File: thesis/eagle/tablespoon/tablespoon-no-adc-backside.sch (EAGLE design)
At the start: 35 parts, among them IC1 7805DT, IC2 7805DT, IC3 TL072D, U2 ADCS7477

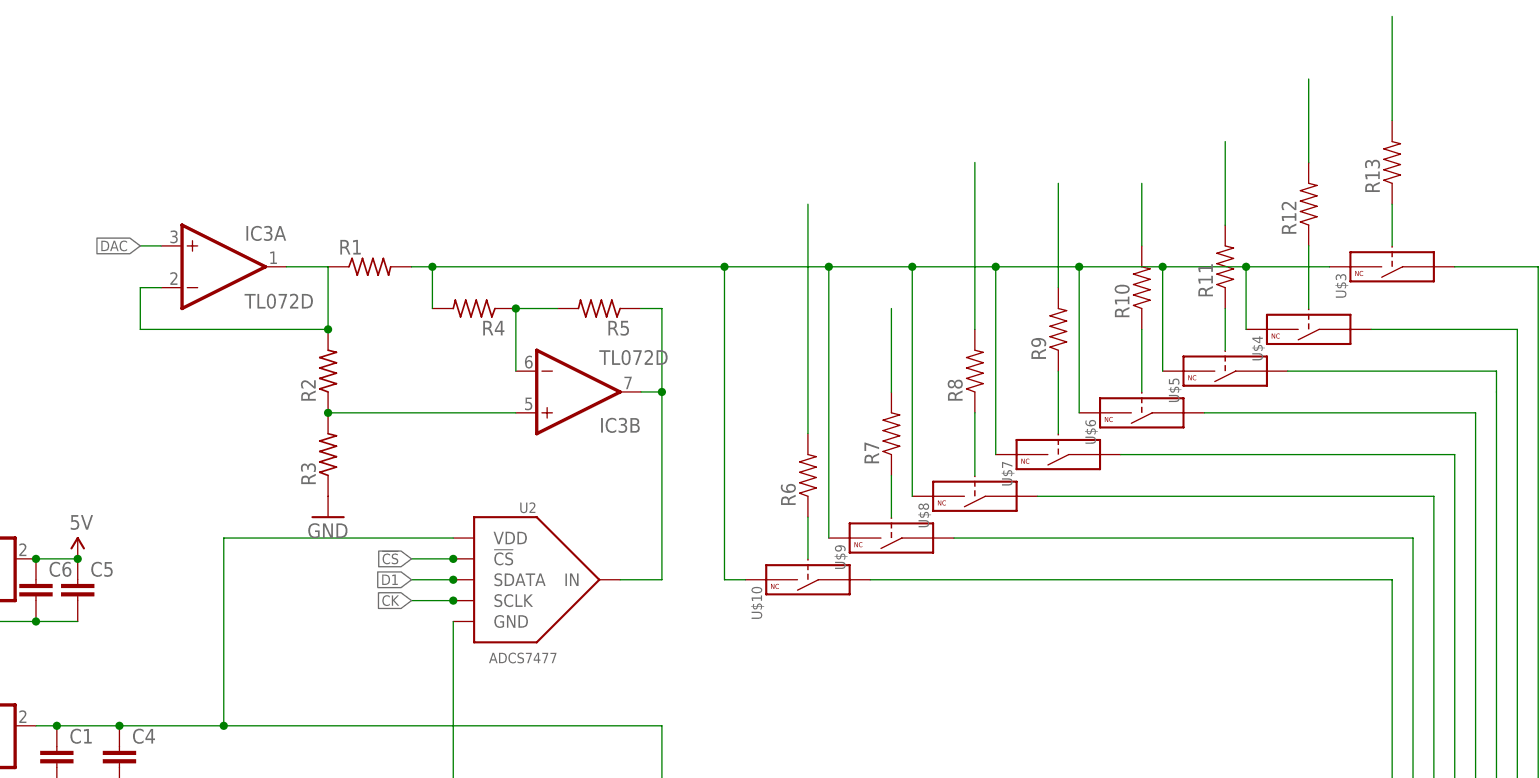
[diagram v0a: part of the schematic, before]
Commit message: fixed lack of resistor divider on current amp
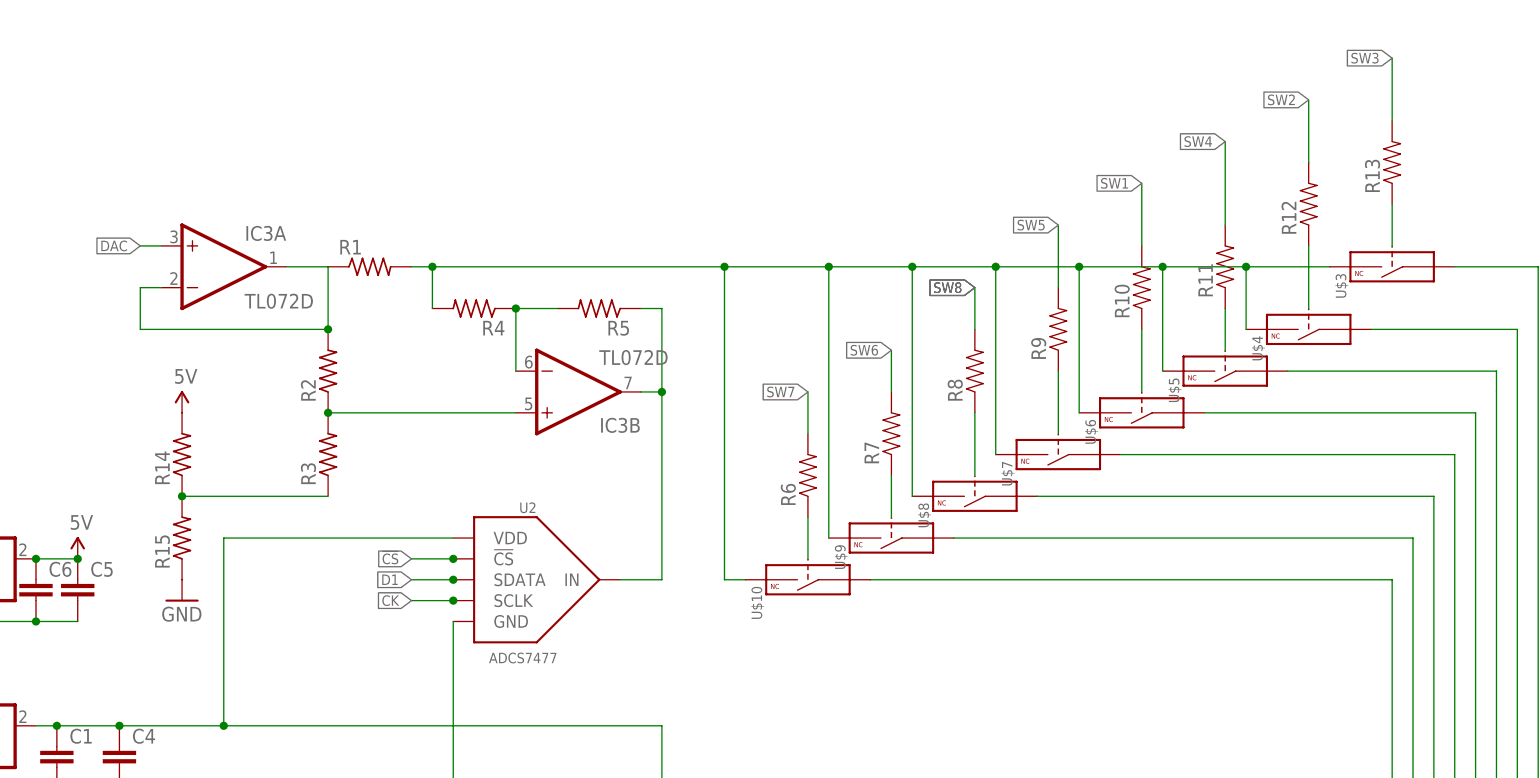
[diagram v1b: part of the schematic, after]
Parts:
- added R14, R15: (no value), rcl:R-US_R0603
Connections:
- new net N$35: R14.1, R15.2, R3.1
- net 5V: now also R14.2
- net GND: now also R15.1; no longer R3.1
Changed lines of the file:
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@@
 <part name="R4" library="rcl" deviceset="R-US_" device="R0603"/>
 <part name="R5" library="rcl" deviceset="R-US_" device="R0603"/>
-<part name="GND7" library="supply1" deviceset="GND" device=""/>
 <part name="U2" library="butter" deviceset="ADCS7477" device=""/>
 <part name="R6" library="SparkFun-Passives" deviceset="RESISTOR" device="0805-RES"/>
@@
 <part name="R10" library="SparkFun-Passives" deviceset="RESISTOR" device="0805-RES"/>
 <part name="GND8" library="supply1" deviceset="GND" device=""/>
+<part name="R14" library="rcl" deviceset="R-US_" device="R0603"/>
+<part name="R15" library="rcl" deviceset="R-US_" device="R0603"/>
+<part name="SUPPLY2" library="SparkFun-Aesthetics" deviceset="5V" device=""/>
+<part name="GND7" library="supply1" deviceset="GND" device=""/>
 </parts>
 <sheets>
@@
 <instance part="R4" gate="G$1" x="81.28" y="134.62" rot="R180"/>
 <instance part="R5" gate="G$1" x="96.52" y="134.62" rot="R180"/>
-<instance part="GND7" gate="1" x="63.5" y="109.22"/>
 <instance part="U2" gate="G$1" x="86.36" y="101.6" rot="MR0"/>
 <instance part="R6" gate="G$1" x="121.92" y="114.3" rot="R90"/>
@@
 <instance part="R10" gate="G$1" x="162.56" y="137.16" rot="R90"/>
 <instance part="GND8" gate="1" x="17.78" y="73.66"/>
+<instance part="R14" gate="G$1" x="45.72" y="116.84" rot="R90"/>
+<instance part="R15" gate="G$1" x="45.72" y="106.68" rot="R90"/>
+<instance part="SUPPLY2" gate="G$1" x="45.72" y="121.92"/>
+<instance part="GND7" gate="1" x="45.72" y="99.06"/>
 </instances>
 <busses>
@@
 <pinref part="IC3" gate="P" pin="V+"/>
 <pinref part="SUPPLY1" gate="G$1" pin="5V"/>
+</segment>
+<segment>
+<pinref part="R14" gate="G$1" pin="2"/>
+<pinref part="SUPPLY2" gate="G$1" pin="5V"/>
 </segment>
 </net>
@@
 </segment>
 <segment>
-<pinref part="R3" gate="G$1" pin="1"/>
-<pinref part="GND7" gate="1" pin="GND"/>
-</segment>
-<segment>
 <wire x1="104.14" y1="55.88" x2="91.44" y2="55.88" width="0.1524" layer="91"/>
 <wire x1="91.44" y1="55.88" x2="91.44" y2="76.2" width="0.1524" layer="91"/>
@@
 <pinref part="GND8" gate="1" pin="GND"/>
 </segment>
+<segment>
+<pinref part="R15" gate="G$1" pin="1"/>
+<pinref part="GND7" gate="1" pin="GND"/>
+</segment>
 </net>
 <net name="N$1" class="0">
@@
 </segment>
 <segment>
-<wire x1="142.24" y1="132.08" x2="142.24" y2="152.4" width="0.1524" layer="91"/>
+<wire x1="142.24" y1="132.08" x2="142.24" y2="137.16" width="0.1524" layer="91"/>
 <pinref part="R8" gate="G$1" pin="2"/>
+<label x="142.24" y="137.16" size="1.27" layer="95" rot="R180" xref="yes"/>
+<label x="142.24" y="137.16" size="1.27" layer="95" rot="R180" xref="yes"/>
 </segment>
 </net>
@@
 </segment>
 <segment>
-<wire x1="121.92" y1="119.38" x2="121.92" y2="147.32" width="0.1524" layer="91"/>
+<wire x1="121.92" y1="119.38" x2="121.92" y2="124.46" width="0.1524" layer="91"/>
 <pinref part="R6" gate="G$1" pin="2"/>
+<label x="121.92" y="124.46" size="1.27" layer="95" rot="R180" xref="yes"/>
 </segment>
 </net>
@@
 </segment>
 <segment>
-<wire x1="132.08" y1="124.46" x2="132.08" y2="134.62" width="0.1524" layer="91"/>
+<wire x1="132.08" y1="124.46" x2="132.08" y2="129.54" width="0.1524" layer="91"/>
 <pinref part="R7" gate="G$1" pin="2"/>
+<label x="132.08" y="129.54" size="1.27" layer="95" rot="R180" xref="yes"/>
 </segment>
 </net>
@@
 </segment>
 <segment>
-<wire x1="152.4" y1="137.16" x2="152.4" y2="149.86" width="0.1524" layer="91"/>
+<wire x1="152.4" y1="137.16" x2="152.4" y2="144.78" width="0.1524" layer="91"/>
 <pinref part="R9" gate="G$1" pin="2"/>
+<label x="152.4" y="144.78" size="1.27" layer="95" rot="R180" xref="yes"/>
 </segment>
 </net>
@@
 <wire x1="172.72" y1="144.78" x2="172.72" y2="154.94" width="0.1524" layer="91"/>
 <pinref part="R11" gate="G$1" pin="2"/>
+<label x="172.72" y="154.94" size="1.27" layer="95" rot="R180" xref="yes"/>
 </segment>
 </net>
@@
 </segment>
 <segment>
-<wire x1="193.04" y1="157.48" x2="193.04" y2="170.18" width="0.1524" layer="91"/>
+<wire x1="193.04" y1="157.48" x2="193.04" y2="165.1" width="0.1524" layer="91"/>
 <pinref part="R13" gate="G$1" pin="2"/>
+<label x="193.04" y="165.1" size="1.27" layer="95" rot="R180" xref="yes"/>
 </segment>
 </net>
@@
 </segment>
 <segment>
-<wire x1="182.88" y1="152.4" x2="182.88" y2="162.56" width="0.1524" layer="91"/>
+<wire x1="182.88" y1="152.4" x2="182.88" y2="160.02" width="0.1524" layer="91"/>
 <pinref part="R12" gate="G$1" pin="2"/>
+<label x="182.88" y="160.02" size="1.27" layer="95" rot="R180" xref="yes"/>
 </segment>
 </net>
@@
 <wire x1="162.56" y1="142.24" x2="162.56" y2="149.86" width="0.1524" layer="91"/>
 <pinref part="R10" gate="G$1" pin="2"/>
+<label x="162.56" y="149.86" size="1.27" layer="95" rot="R180" xref="yes"/>
 </segment>
 </net>
@@
 </segment>
 </net>
+<net name="N$35" class="0">
+<segment>
+<pinref part="R3" gate="G$1" pin="1"/>
+<wire x1="63.5" y1="111.76" x2="45.72" y2="111.76" width="0.1524" layer="91"/>
+<pinref part="R14" gate="G$1" pin="1"/>
+<pinref part="R15" gate="G$1" pin="2"/>
+<junction x="45.72" y="111.76"/>
+</segment>
+</net>

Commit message: going for the full-system on one board!
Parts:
- added M1, M2, M3, M4, M5, M6, M7, M8: (no value), butter:N-FET
- added R16, R17: (no value), SparkFun-Passives:RESISTOR0805-RES
- added U$11: 4051", butter:4051"
- added U$2: RAILSEP, butter:RAILSEP
- added U1: ADCS7477, butter:ADCS7477
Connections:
- removed net N$10: JP1.3, U$8G$1.COM
- removed net N$11: JP1.1, U$10G$1.COM
- removed net N$12: JP1.2, U$9G$1.COM
- removed net N$27: JP1.6, U$5G$1.COM
- removed net N$28: JP1.7, U$4G$1.COM
- new net N$1: JP1.2, M7.D, U$11.Y0, U$9G$1.COM
- new net N$36: R16.2, R17.2, U$10G$2.VCC, U$3G$2.VCC, U$4G$2.VCC, U$5G$2.VCC, U$6G$2.VCC, U$7G$2.VCC, U$8G$2.VCC, U$9G$2.VCC
- new net N$37: U$11.Z, U1.IN
- new net N$38: JP1.7, M2.D, U$11.Y7, U$4G$1.COM
- new net N$39: JP1.6, M3.D, U$11.Y6, U$5G$1.COM
- new net N$40: JP1.5, M4.D, U$11.Y4, U$6G$1.COM
- new net N$41: JP1.4, M5.D, U$11.Y2, U$7G$1.COM
- net !CS: now also U$1.PA0, U1.!CS; no longer U$1.PC13
- net 4.6V: now also R16.1; no longer U$10G$2.VCC, U$3G$2.VCC, U$4G$2.VCC, U$5G$2.VCC, U$6G$2.VCC, U$7G$2.VCC, U$8G$2.VCC, U$9G$2.VCC
- net 5V: now also R17.1, U$11.VCC
- net CK: now also U1.SCLK
- net D0: now also U1.SDATA
- net G0: now also M1.G
- net G1: now also M2.G
- net G2: now also M3.G
- net G3: now also M4.G
- net G4: now also M5.G
- net G5: now also M6.G
- net G6: now also M7.G
- net G7: now also M8.G
- net GND: now also M1.S, M2.S, M3.S, M4.S, M5.S, M6.S, M7.S, M8.S, U$11.GND, U$11.VEE, U1.GND
- net N$2: now also U1.VDD
- net N$29: now also M1.D, U$11.Y5
- net N$6: now also JP1.3, M6.D, U$11.Y1, U$8G$1.COM; no longer JP1.4, U$7G$1.COM
- net N$9: now also JP1.1, M8.D, U$10G$1.COM, U$11.Y3; no longer JP1.5, U$6G$1.COM
- net S0: now also U$11.S0
- net S1: now also U$11.S1
- net S2: now also U$11.S2
- net SE: now also U$11.!E

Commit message: finished new board
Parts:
- added JP2: POWER_JACKPTH, SparkFun-Connectors:POWER_JACKPTH
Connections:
- net GND: now also JP2.GND, JP2.GNDBREAK, U$1.GND, U$1.GND1, U$1.GND4, U$1.GND5
- net N$5: now also JP2.PWR
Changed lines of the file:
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@@
 <part name="SUPPLY6" library="SparkFun-Aesthetics" deviceset="5V" device=""/>
 <part name="GND21" library="supply1" deviceset="GND" device=""/>
+<part name="JP2" library="SparkFun-Connectors" deviceset="POWER_JACK" device="PTH"/>
+<part name="GND22" library="supply1" deviceset="GND" device=""/>
+<part name="GND23" library="supply1" deviceset="GND" device=""/>
+<part name="GND24" library="supply1" deviceset="GND" device=""/>
+<part name="GND25" library="supply1" deviceset="GND" device=""/>
+<part name="GND26" library="supply1" deviceset="GND" device=""/>
 </parts>
 <sheets>
@@
 <instance part="SUPPLY6" gate="G$1" x="162.56" y="66.04"/>
 <instance part="GND21" gate="1" x="154.94" y="63.5"/>
+<instance part="JP2" gate="G$1" x="-17.78" y="76.2"/>
+<instance part="GND22" gate="1" x="-12.7" y="76.2"/>
+<instance part="GND23" gate="1" x="27.94" y="0"/>
+<instance part="GND24" gate="1" x="2.54" y="0"/>
+<instance part="GND25" gate="1" x="2.54" y="66.04" rot="R180"/>
+<instance part="GND26" gate="1" x="27.94" y="66.04" rot="R180"/>
 </instances>
 <busses>
@@
 <wire x1="154.94" y1="68.58" x2="154.94" y2="66.04" width="0.1524" layer="91"/>
 </segment>
+<segment>
+<pinref part="JP2" gate="G$1" pin="GND"/>
+<pinref part="GND22" gate="1" pin="GND"/>
+<wire x1="-15.24" y1="78.74" x2="-12.7" y2="78.74" width="0.1524" layer="91"/>
+<pinref part="JP2" gate="G$1" pin="GNDBREAK"/>
+<wire x1="-15.24" y1="81.28" x2="-12.7" y2="81.28" width="0.1524" layer="91"/>
+<wire x1="-12.7" y1="81.28" x2="-12.7" y2="78.74" width="0.1524" layer="91"/>
+<junction x="-12.7" y="78.74"/>
+</segment>
+<segment>
+<pinref part="U$1" gate="G$1" pin="GND5"/>
+<pinref part="GND23" gate="1" pin="GND"/>
+</segment>
+<segment>
+<pinref part="U$1" gate="G$1" pin="GND4"/>
+<pinref part="GND24" gate="1" pin="GND"/>
+</segment>
+<segment>
+<pinref part="U$1" gate="G$1" pin="GND"/>
+<pinref part="GND25" gate="1" pin="GND"/>
+</segment>
+<segment>
+<pinref part="U$1" gate="G$1" pin="GND1"/>
+<pinref part="GND26" gate="1" pin="GND"/>
+</segment>
 </net>
 <net name="S0" class="0">
@@
 <junction x="-5.08" y="83.82"/>
 <wire x1="-15.24" y1="83.82" x2="-5.08" y2="83.82" width="0.1524" layer="91"/>
-</segment>
-</net>
+<pinref part="JP2" gate="G$1" pin="PWR"/>
+<junction x="-15.24" y="83.82"/>
+</segment>
+</net>
